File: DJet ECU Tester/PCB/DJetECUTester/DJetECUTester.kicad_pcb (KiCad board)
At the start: 2 copper layers, 89 parts, among them J1 ISP, J2 ECU, J3 USB_B_Mini, J4 BREAKOUT, J5 12V IN, J6 MPS, J7 VAC, Q1 MMBT2222ALT1G, Q10 MMBT2222ALT1G, Q2 MMBT2222ALT1G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

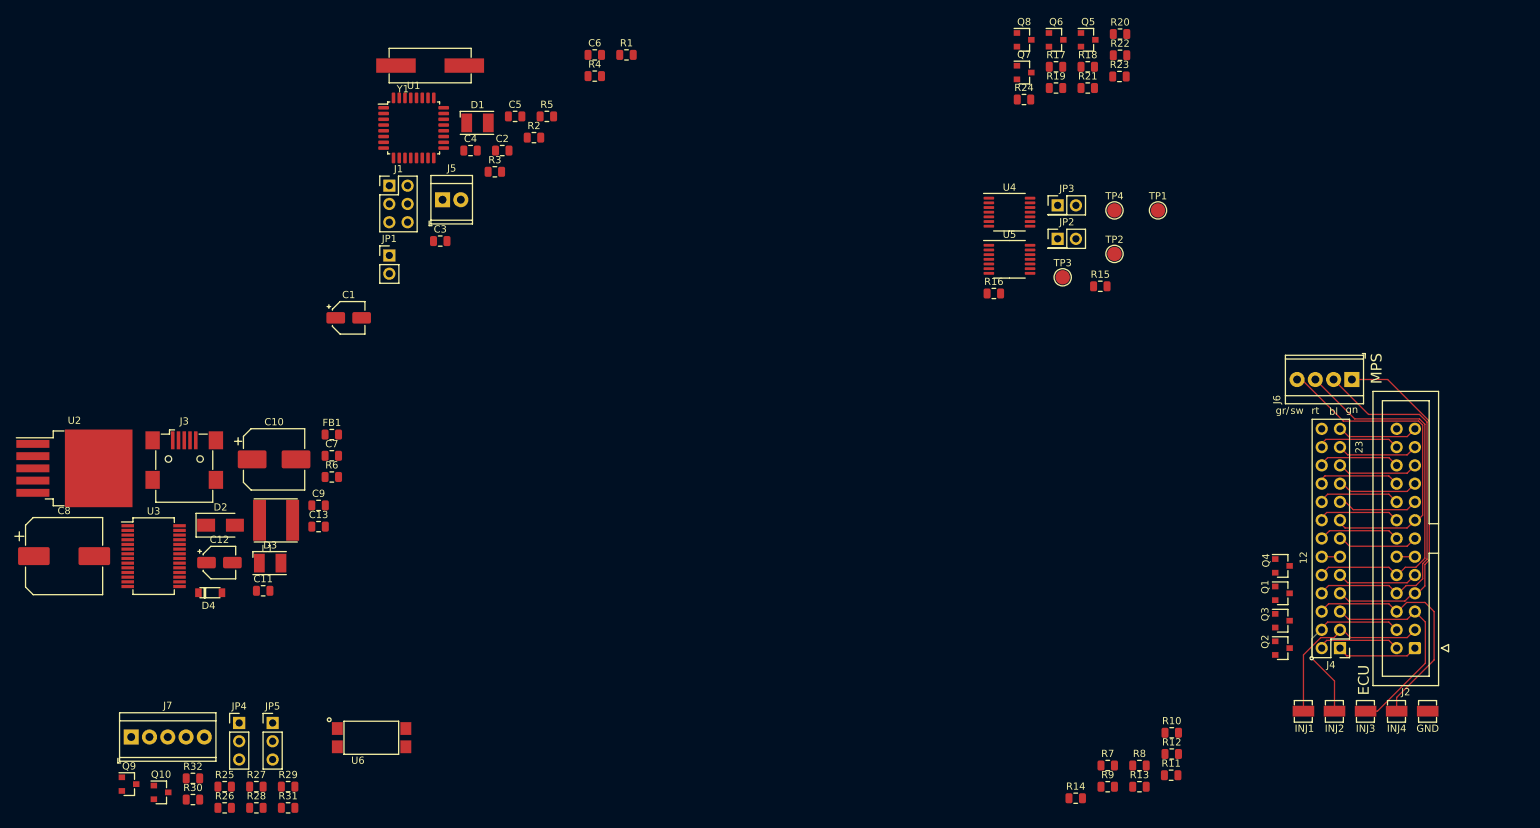
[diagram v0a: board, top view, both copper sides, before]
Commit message: Working on PCB layout. Changed CSV circuit from optocoupler to transistors. Added decoupling caps for digital pots.
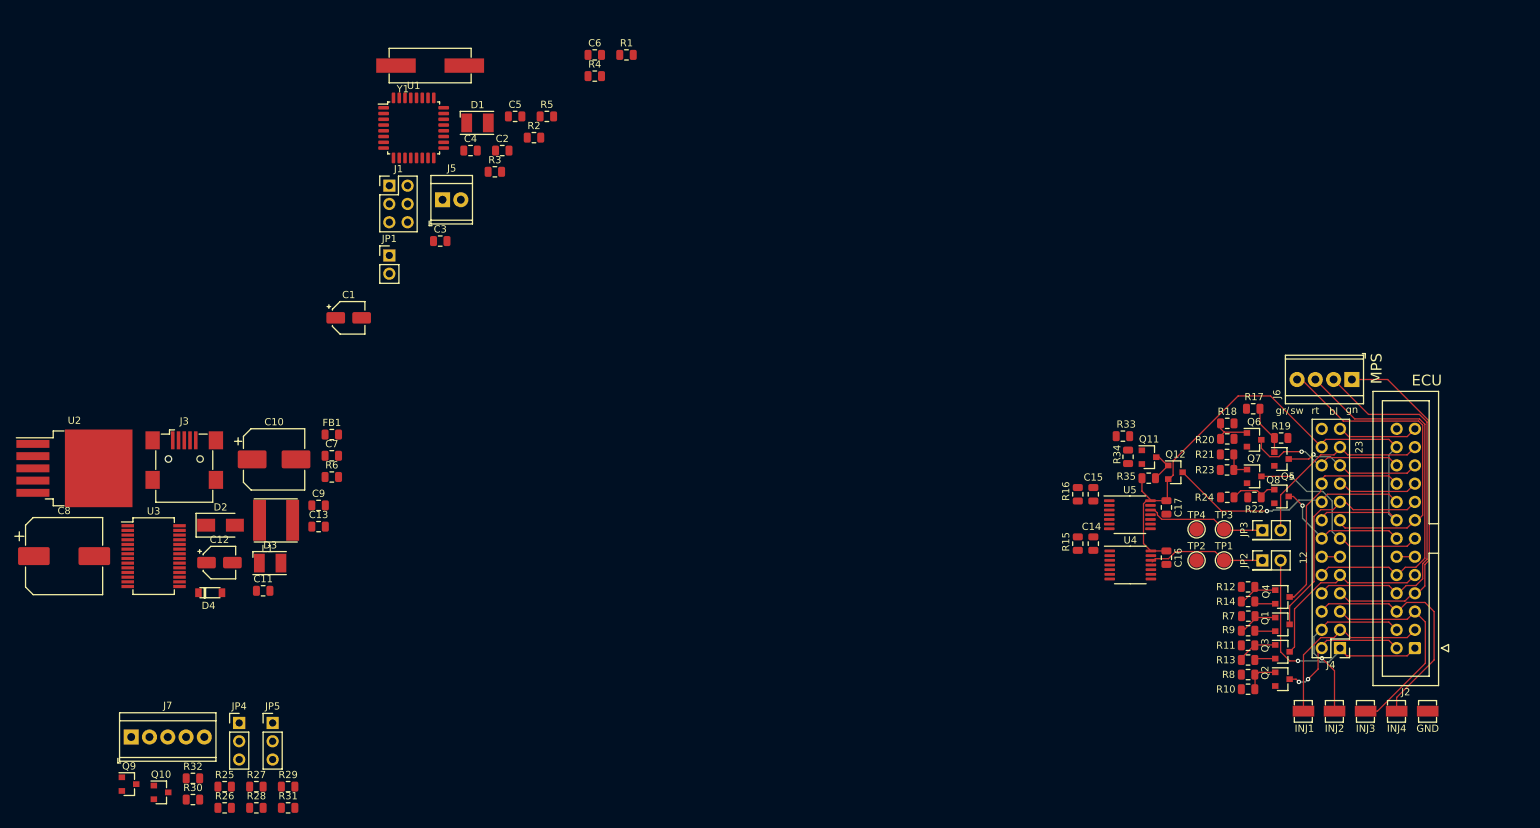
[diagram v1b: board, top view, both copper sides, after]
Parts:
- removed U6: SFH617A-1X007T, Britishideas:SMD-4-OPTION7
- added C14: 100nF, Capacitor_SMD:C_0805_2012Metric, F.Cu at (208.4, 99.5)
- added C15: 100nF, Capacitor_SMD:C_0805_2012Metric, F.Cu at (208.4, 92.7)
- added C16: 100nF, Capacitor_SMD:C_0805_2012Metric, F.Cu at (218.6, 101.5)
- added C17: 100nF, Capacitor_SMD:C_0805_2012Metric, F.Cu at (218.6, 94.5)
- added Q11: MMBT2222ALT1G, Package_TO_SOT_SMD:SOT-23, F.Cu at (216.2, 87.5)
- added Q12: MMBT3906LT1G, Package_TO_SOT_SMD:SOT-23, F.Cu at (219.8, 89.6)
- added R33: 1k, Resistor_SMD:R_0805_2012Metric, F.Cu at (212.5, 84.6)
- added R34: 10k, Resistor_SMD:R_0805_2012Metric, F.Cu at (213.2, 87.5)
- added R35: 10k, Resistor_SMD:R_0805_2012Metric, F.Cu at (216.1, 90.4)
- moved Q8 72.9 mm to (234.6, 93.0)
- moved Q7 64.6 mm to (230.8, 90.2)
- moved R22 64.2 mm to (230.8, 93.1), turned to 180 degrees
- moved Q5 64.2 mm to (234.6, 87.8)
- moved R24 62.1 mm to (227.0, 93.1), turned to 180 degrees
- moved Q6 62.0 mm to (230.8, 85.1)
- moved R20 58.2 mm to (227.0, 85.0)
- moved R19 57.9 mm to (234.5, 84.8)
- moved R23 56.7 mm to (227.0, 89.3), turned to 180 degrees
- moved R17 54.9 mm to (230.6, 80.8), turned to 180 degrees
- moved R21 54.5 mm to (227.0, 87.1), turned to 180 degrees
- moved JP3 53.4 mm to (231.9, 97.7)
- moved R18 53.2 mm to (227.0, 82.8)
- moved JP2 53.0 mm to (231.9, 101.9)
- moved U4 51.8 mm to (213.5, 102.5)
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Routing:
- net +12V: track 22.6 -> 82.4 mm
- net /ECU_COLDSTARTRELAY: track 11.4 -> 33.5 mm, vias 0 -> 1
- net /ECU_AIRTEMP: track 11.4 -> 33.3 mm, vias 0 -> 1
- net /ECU_TPSIDLE: track 11.1 -> 31.7 mm
- net /ECU_TPSACCEL2: track 11.4 -> 28.7 mm
- net /ECU_TRIGGERGROUP2: track 10.5 -> 27.2 mm, vias 0 -> 1
- net Net-(JP3-Pad1): track 0.00 -> 16.5 mm
- net Net-(JP2-Pad1): track 0.00 -> 16.3 mm
- net /ECU_COOLANTTEMP: track 11.3 -> 26.9 mm
- net /ECU_TPSACCEL1: track 10.9 -> 25.1 mm
- net /ECU_TRIGGERGROUP3: track 11.2 -> 22.0 mm, vias 0 -> 1
- net GND: track 5.01 -> 13.6 mm
- net /ECU_TRIGGERGROUP4: track 10.6 -> 18.4 mm, vias 0 -> 1
- net /ECU_TRIGGERGROUP1: track 11.2 -> 18.7 mm, vias 0 -> 1
- net /ECU_TPSWOT: track 11.3 -> 18.7 mm, vias 0 -> 2
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
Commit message: Working on PCB layout
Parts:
- removed JP5: VAC2 VSEL, Connector_PinHeader_2.54mm:PinHeader_1x03_P2.54mm_Vertical
- added Q13: MMBT3906LT1G, Package_TO_SOT_SMD:SOT-23, F.Cu at (184.7, 122.9)
- added Q14: MMBT3906LT1G, Package_TO_SOT_SMD:SOT-23, F.Cu at (195.3, 107.1)
- added R36: 10k, Resistor_SMD:R_0805_2012Metric, F.Cu at (185.4, 119.0)
- added R37: 10k, Resistor_SMD:R_0805_2012Metric, F.Cu at (190.8, 107.1)
- J7: footprint TerminalBlock_TE-Connectivity:TerminalBlock_TE_282834-5_1x05_P2.54mm_Horizontal -> TerminalBlock_TE-Connectivity:TerminalBlock_TE_282834-6_1x06_P2.54mm_Horizontal
- JP4: value VAC1 VSEL -> VAC VCC
- R29, R30: value 100k -> 10k
- R31, R32: value 100k -> 1k
- Y1: value ECS-160-18-5PX-TR 16MHz -> FA-238 16.0000MB-C3; footprint Britishideas:HC-49_US -> Britishideas:FA-238
- moved C8 146.5 mm to (209.0, 72.6), turned to 180 degrees
- moved Y1 133.2 mm to (216.3, 121.0), turned to 270 degrees
- moved U2 127.1 mm to (193.0, 74.3), turned to 180 degrees
- moved C1 124.2 mm to (222.1, 109.2), turned to 90 degrees
- moved C4 123.5 mm to (219.9, 120.0)
- moved C5 123.1 mm to (219.9, 122.0), turned to 180 degrees
- moved U1 121.6 mm to (210.9, 115.1), turned to 90 degrees
- moved Q9 119.4 mm to (193.4, 124.1), turned to 270 degrees
- moved Q10 118.3 mm to (195.3, 113.9), turned to 90 degrees
- moved R30 116.3 mm to (197.0, 111.0), turned to 180 degrees
- moved C6 115.4 mm to (210.4, 122.3), turned to 270 degrees
- moved C3 114.9 mm to (212.5, 122.3), turned to 270 degrees
- moved U3 113.2 mm to (190.2, 88.8), turned to 180 degrees
- moved R32 112.1 mm to (193.4, 111.0)
- moved JP1 111.0 mm to (203.5, 120.3), turned to 270 degrees
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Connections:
- J7 pad 1: +5V -> /Vacuum/VACVCC
- J7 pad 2: +12V -> Net-(J7-Pad2)
- J7 pad 5: GND -> Net-(J7-Pad5)
- JP4 pad 1: Net-(JP4-Pad1) -> +12V
- JP4 pad 2: Net-(J7-Pad3) -> /Vacuum/VACVCC
- JP4 pad 3: Net-(JP4-Pad3) -> +5V
- Q9 pad 3: Net-(J7-Pad3) -> Net-(J7-Pad2)
- R29 pad 1: +12V -> /Vacuum/VACVCC
- R29 pad 2: Net-(JP4-Pad1) -> Net-(J7-Pad2)
- R30 pad 1: +12V -> /Vacuum/VACVCC
- R30 pad 2: Net-(JP5-Pad1) -> Net-(J7-Pad4)
- R31 pad 1: +5V -> Net-(Q13-Pad1)
- R31 pad 2: Net-(JP4-Pad3) -> Net-(J7-Pad2)
- R32 pad 1: +5V -> Net-(Q14-Pad1)
- R32 pad 2: Net-(JP5-Pad3) -> Net-(J7-Pad4)
- Y1 pad 1: Net-(C5-Pad2) -> Net-(C4-Pad1)
- Y1 pad 2: Net-(C4-Pad1) -> GND
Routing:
- net +5V: track 0.00 -> 188.9 mm, vias 0 -> 10
- net +12V: track 82.4 -> 165.7 mm, vias 0 -> 2
- net /TRIGGERGROUP2: track 0.00 -> 47.9 mm, vias 0 -> 2
- net /Vacuum/VACVCC: track 0.00 -> 47.5 mm, vias 0 -> 2
- net /TRIGGERGROUP1: track 0.00 -> 47.1 mm, vias 0 -> 2
- net /TRIGGERGROUP4: track 0.00 -> 45.9 mm, vias 0 -> 4
- net /TX: track 0.00 -> 45.4 mm, vias 0 -> 2
- net /CSV: track 0.00 -> 43.6 mm, vias 0 -> 2
- net /TRIGGERGROUP3: track 0.00 -> 39.2 mm, vias 0 -> 2
- net /SCK: track 0.00 -> 38.1 mm, vias 0 -> 5
- net /RX: track 0.00 -> 37.0 mm, vias 0 -> 2
- net /MOSI: track 0.00 -> 33.5 mm, vias 0 -> 5
- net /~RESET: track 0.00 -> 32.1 mm, vias 0 -> 3
- net /MISO: track 0.00 -> 31.8 mm, vias 0 -> 3
- net Net-(J7-Pad5): track 0.00 -> 29.9 mm, vias 0 -> 2
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- added copper zone on B.Cu, net GND
- added copper zone on F.Cu, net GND
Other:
- board outline added: 83.5 x 60 mm
- board text added: "(C) ANDY@BRITISHIDEAS.COM 2021"
- board text added: "1"
- board text added: "10"
- board text added: "12V"
- board text added: "13"
- board text added: "14"
- board text added: "17"
- board text added: "18"
- board text added: "2"
- board text added: "21"
- board text added: "22"
- board text added: "25"
- board text added: "3"
- board text added: "4"
- board text added: "5"
- board text added: "6"
- board text added: "9"
- board text added: "BRKOUT"
- board text added: "G"
- board text added: "MERCEDES V8 DJET ECU TESTER V1"
- board text added: "PWR"
- board text added: "STATUS"
- board text added: "VAC"
- board text added: "X"
- board text added: "grey+"
- board text removed: "12"
- board text removed: "23"
- board text removed: "gr/"

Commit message: Added final 3D models.
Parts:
- TP5, TP6, TP7, TP8: value 5190TR -> 5194TR
- TP9: value 5190TR -> 5195TR

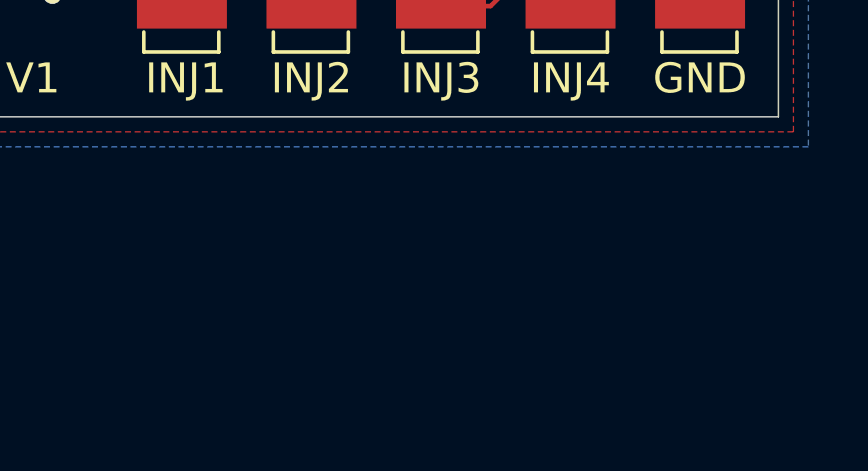
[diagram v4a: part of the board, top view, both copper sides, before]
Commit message: Added simulation of injector drivers - only 1-5 group tested.
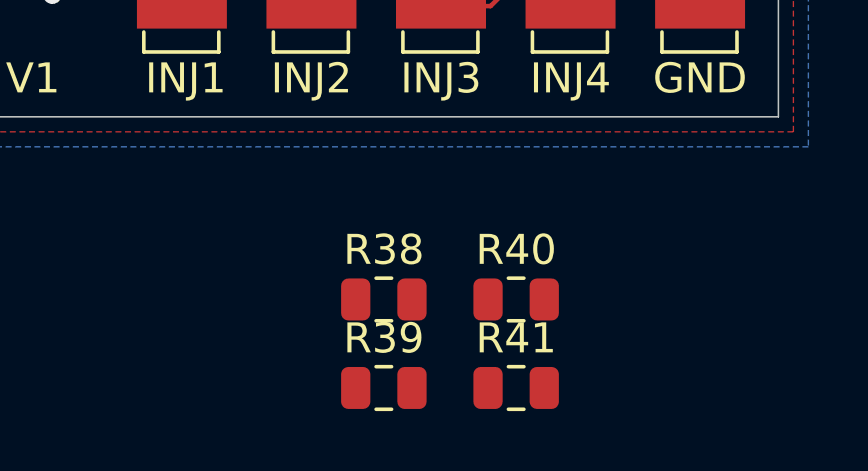
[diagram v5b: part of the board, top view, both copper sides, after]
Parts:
- added R38: 2.4, Resistor_SMD:R_0805_2012Metric, F.Cu at (244.3, 132.6)
- added R39: 2.4, Resistor_SMD:R_0805_2012Metric, F.Cu at (244.3, 135.5)
- added R40: 2.4, Resistor_SMD:R_0805_2012Metric, F.Cu at (248.8, 132.6)
- added R41: 2.4, Resistor_SMD:R_0805_2012Metric, F.Cu at (248.8, 135.5)

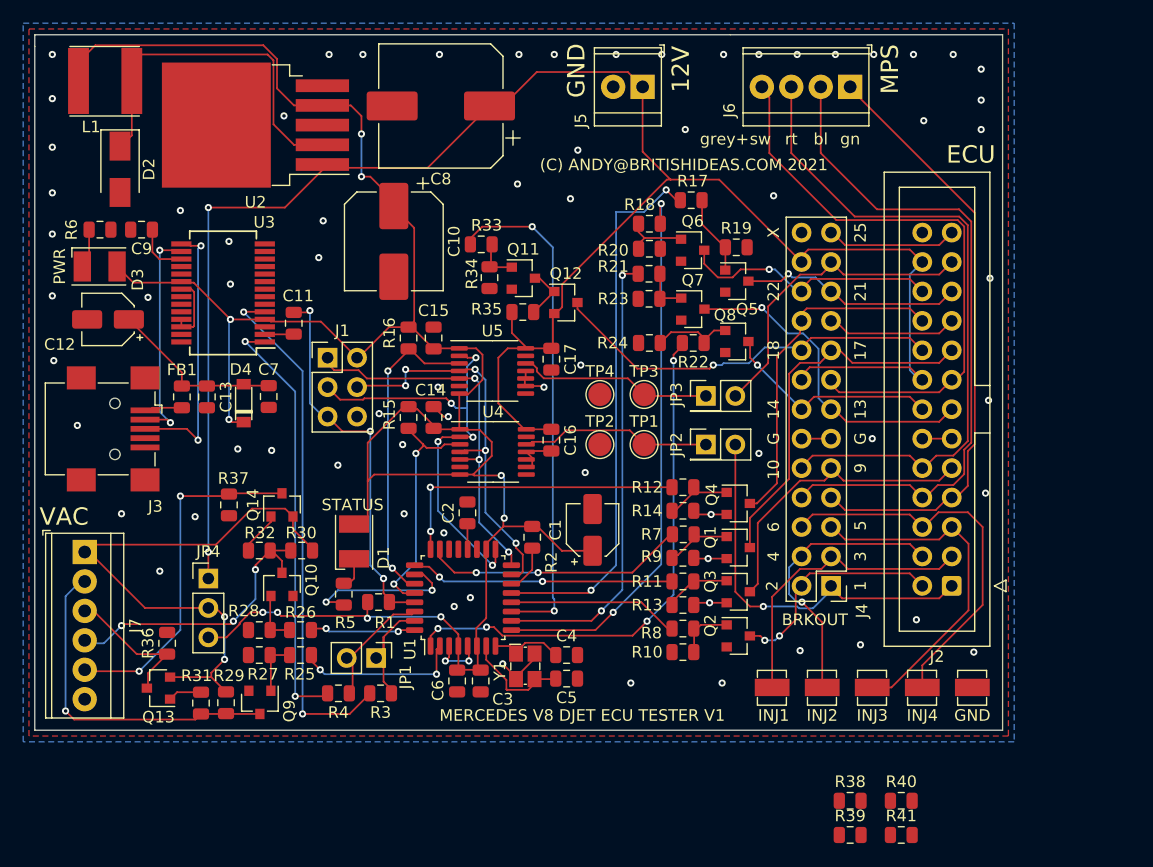
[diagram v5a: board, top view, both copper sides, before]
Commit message: Added connector for injector groups.
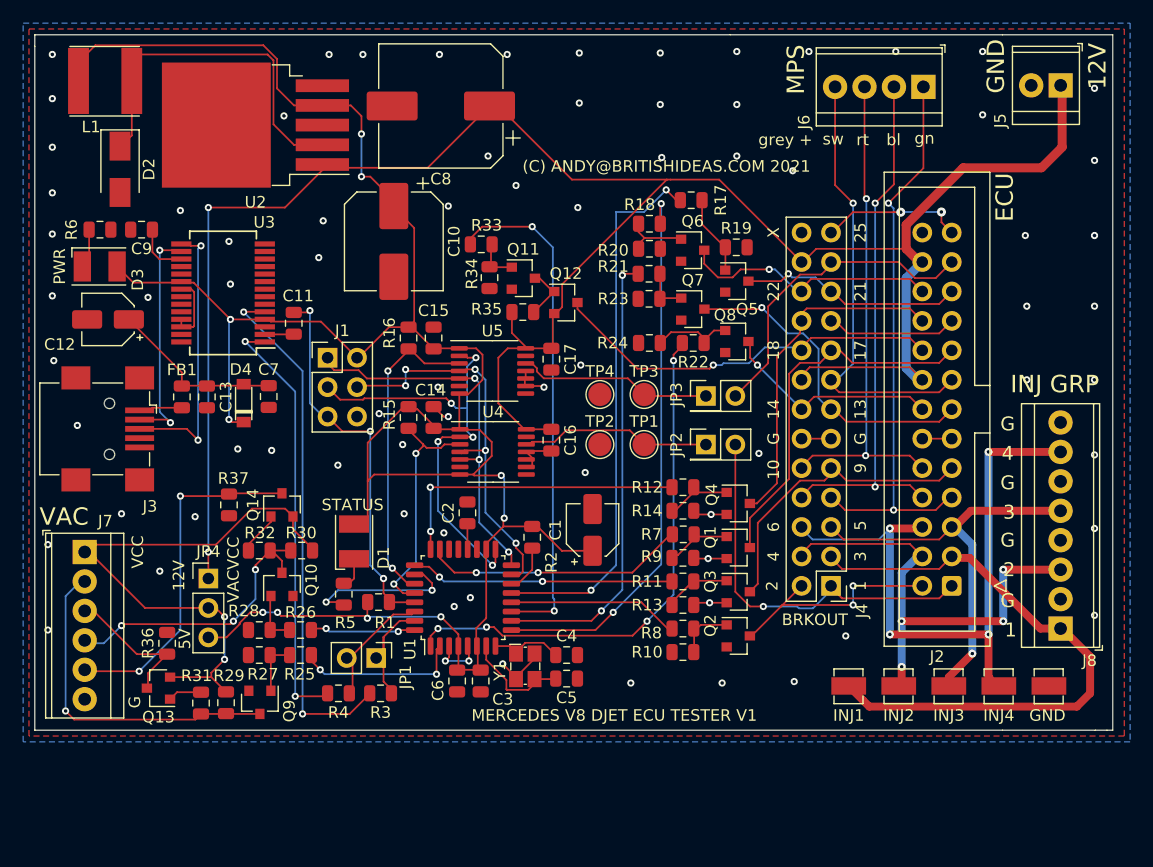
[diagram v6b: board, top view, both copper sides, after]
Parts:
- removed R38, R39, R40, R41: 2.4, Resistor_SMD:R_0805_2012Metric
- added J8: INJECTORS, TerminalBlock_TE-Connectivity:TerminalBlock_TE_282834-8_1x08_P2.54mm_Horizontal, F.Cu at (262.5, 117.7)
- moved J5 36.1 mm to (262.5, 70.9)
- moved TP5 6.61 mm to (244.2, 122.7)
- moved TP7 6.61 mm to (252.9, 122.7)
- moved TP8 6.61 mm to (257.2, 122.7)
- moved TP6 6.61 mm to (248.5, 122.7)
- moved TP9 6.61 mm to (261.5, 122.7)
- moved J6 6.32 mm to (250.7, 71.0)
- moved J3 0.47 mm to (180.4, 100.5)
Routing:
- net /ECU_INJGROUP1: track 25.3 -> 51.2 mm
- net /ECU_INJGROUP4: track 33.4 -> 54.9 mm, vias 0 -> 4
- net +12V: track 165.7 -> 182.9 mm
- net /ECU_INJGROUP2: track 24.5 -> 41.0 mm, vias 1 -> 4
- net /MPS-10: track 56.6 -> 42.6 mm, vias 0 -> 2
- net /MPS-15: track 49.6 -> 37.5 mm, vias 0 -> 1
- net /MPS-8: track 57.9 -> 46.8 mm, vias 0 -> 2
- net /ECU_INJGROUP3: track 29.7 -> 36.4 mm, vias 0 -> 1
- net /MPS-7: track 50.9 -> 48.9 mm, vias 0 -> 2
- net /ECU_TPSWOT: track 18.7 -> 20.3 mm
- net /ECU_DIAGGROUP13: track 11.4 -> 12.3 mm, vias 0 -> 2
- net GND: vias 72 -> 77
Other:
- board size 83.5 x 60 mm -> 93 x 60 mm
- net class Injectors added: clearance 0.1524, trace_width 0.684, via_dia 0.62, via_drill 0.3
- board text added: "5V"
- board text added: "INJ GRP"
- board text added: "VACVCC"
- board text added: "VCC"
- board text added: "grey +"
- board text removed: "grey+"
